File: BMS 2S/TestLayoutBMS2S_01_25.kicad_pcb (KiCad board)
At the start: 2 copper layers, 20 parts

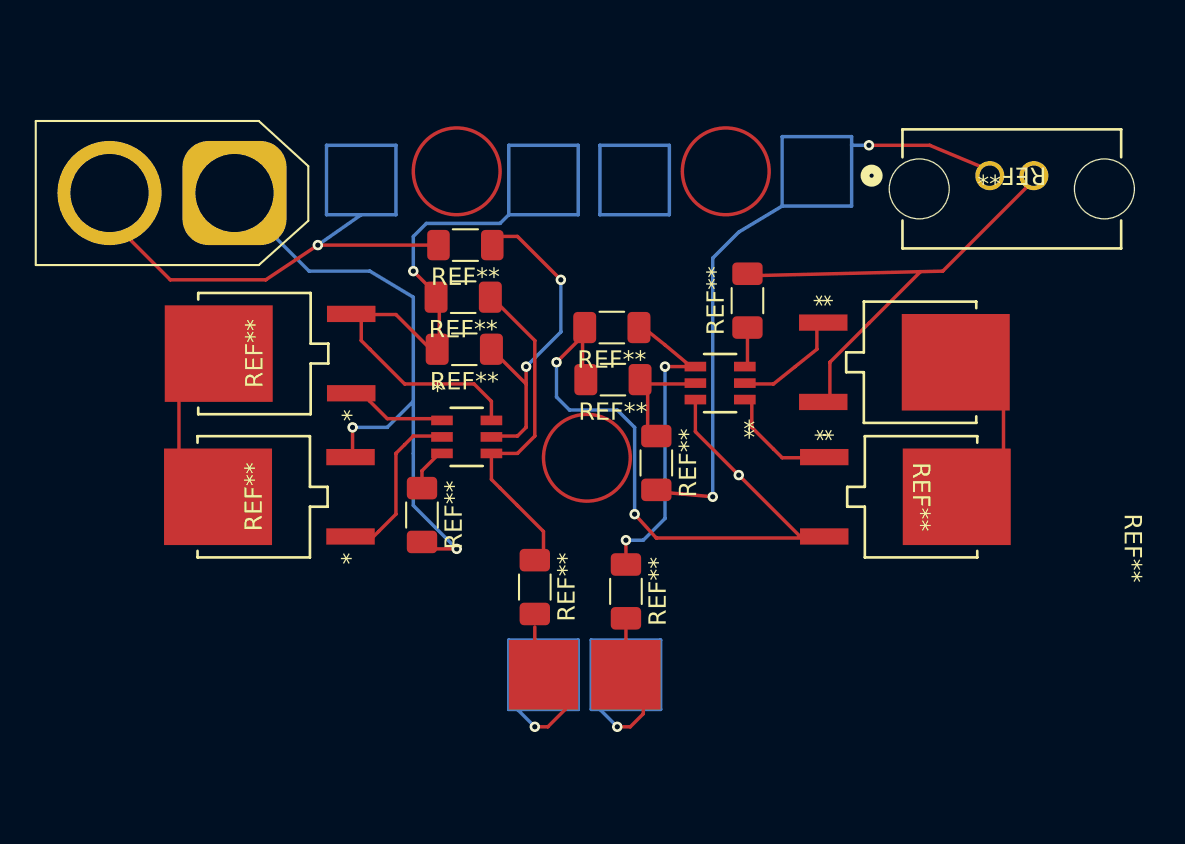
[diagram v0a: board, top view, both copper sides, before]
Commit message: BMS 2S, ajustement du design
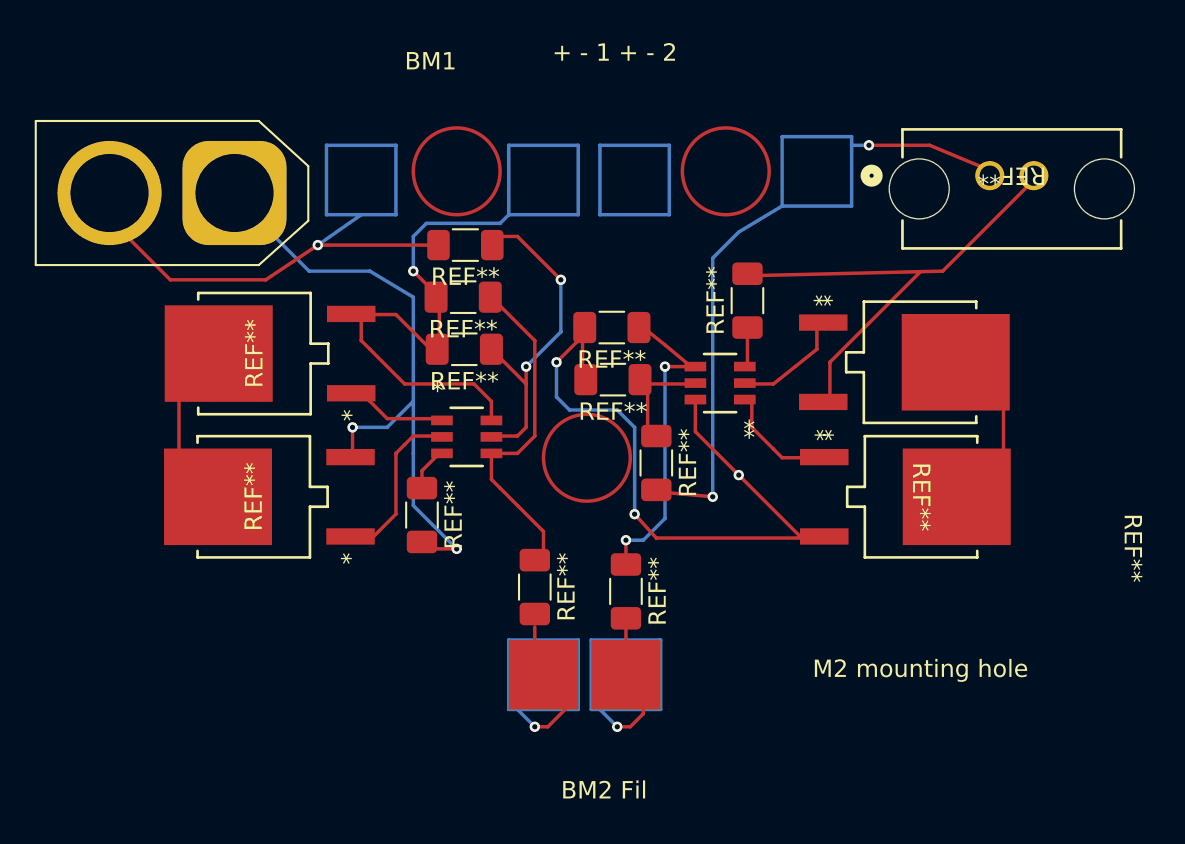
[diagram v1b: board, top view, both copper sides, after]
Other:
- board text added: "+ - 1 + - 2"
- board text added: "BM1"
- board text added: "BM2 Fil"
- board text added: "M2 mounting hole"
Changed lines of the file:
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@@
 		(layer "Cmts.User")
+	)
+	(gr_text "BM2 Fil"
+		(at 133 124 0)
+		(layer "F.SilkS")
+		(effects
+			(font
+				(size 1 1)
+				(thickness 0.1)
+			)
+			(justify left bottom)
+		)
+	)
+	(gr_text "M2 mounting hole"
+		(at 147.5 117 0)
+		(layer "F.SilkS")
+		(effects
+			(font
+				(size 1 1)
+				(thickness 0.1)
+			)
+			(justify left bottom)
+		)
+	)
+	(gr_text "BM1\n"
+		(at 124 82 0)
+		(layer "F.SilkS")
+		(effects
+			(font
+				(size 1 1)
+				(thickness 0.1)
+			)
+			(justify left bottom)
+		)
+	)
+	(gr_text "+ - 1 + - 2\n"
+		(at 132.5 81.5 0)
+		(layer "F.SilkS")
+		(effects
+			(font
+				(size 1 1)
+				(thickness 0.1)
+			)
+			(justify left bottom)
+		)
 	)
 	(gr_text "B-2\n\n"
